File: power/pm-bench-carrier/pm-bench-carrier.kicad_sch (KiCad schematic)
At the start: 41 parts, among them J1 VIN 40-60V, J2 VOUT 19V, Q1 2N7002, X1 PM-19V-200W, X2 Aux socket

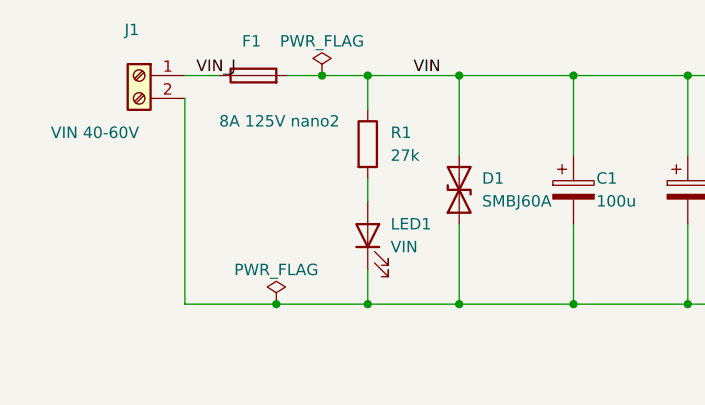
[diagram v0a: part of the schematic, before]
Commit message: pm-bench-carrier: LCSC numbers on the SMD parts, fuse 10 A (0451010.MRL); jlcfab BOM/CPL filled
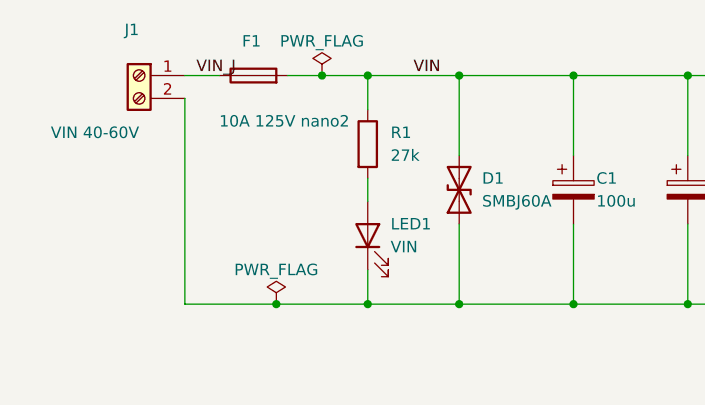
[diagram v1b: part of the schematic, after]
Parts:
- C3: LCSC (none) -> C55151
- C5: LCSC (none) -> C2918502
- C6: LCSC (none) -> C15849
- D1: LCSC (none) -> C353345
- D2: LCSC (none) -> C27131
- F1: value 8A 125V nano2 -> 10A 125V nano2; LCSC (none) -> C44479
- LED1, LED2, LED4: LCSC (none) -> C2297
- LED3: LCSC (none) -> C84256
- Q1: LCSC (none) -> C8545
- R1: LCSC (none) -> C17943
- R2: LCSC (none) -> C17414
- R3: LCSC (none) -> C270956
- R4, R6: LCSC (none) -> C25803
- R5, R7: LCSC (none) -> C22978
- R8, R9: LCSC (none) -> C25804
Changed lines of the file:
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@@
 			)
 		)
-		(property "Value" "8A 125V nano2"
+		(property "Value" "10A 125V nano2"
 			(at 39.37 55.88 270)
 			(show_name no)
@@
 			)
 		)
+		(property "LCSC" "C44479"
+			(at 43.18 50.8 0)
+			(show_name no)
+			(do_not_autoplace no)
+			(hide yes)
+			(effects
+				(font
+					(size 1.27 1.27)
+				)
+			)
+		)
 		(pin "1"
 		)
@@
 			)
 		)
+		(property "LCSC" "C353345"
+			(at 66.04 63.5 0)
+			(show_name no)
+			(do_not_autoplace no)
+			(hide yes)
+			(effects
+				(font
+					(size 1.27 1.27)
+				)
+			)
+		)
 		(pin "1"
 		)
@@
 			)
 		)
+		(property "LCSC" "C55151"
+			(at 101.6 63.5 0)
+			(show_name no)
+			(do_not_autoplace no)
+			(hide yes)
+			(effects
+				(font
+					(size 1.27 1.27)
+				)
+			)
+		)
 		(pin "1"
 		)
@@
 			)
 		)
+		(property "LCSC" "C17943"
+			(at 55.88 58.42 0)
+			(show_name no)
+			(do_not_autoplace no)
+			(hide yes)
+			(effects
+				(font
+					(size 1.27 1.27)
+				)
+			)
+		)
 		(pin "1"
 		)
@@
 			)
 		)
+		(property "LCSC" "C2297"
+			(at 55.88 68.58 0)
+			(show_name no)
+			(do_not_autoplace no)
+			(hide yes)
+			(effects
+				(font
+					(size 1.27 1.27)
+				)
+			)
+		)
 		(pin "1"
 		)
@@
 			)
 		)
+		(property "LCSC" "C2918502"
+			(at 187.96 63.5 0)
+			(show_name no)
+			(do_not_autoplace no)
+			(hide yes)
+			(effects
+				(font
+					(size 1.27 1.27)
+				)
+			)
+		)
 		(pin "1"
 		)
@@
 			)
 		)
+		(property "LCSC" "C17414"
+			(at 198.12 58.42 0)
+			(show_name no)
+			(do_not_autoplace no)
+			(hide yes)
+			(effects
+				(font
+					(size 1.27 1.27)
+				)
+			)
+		)
 		(pin "1"
 		)
@@
 			)
 		)
+		(property "LCSC" "C2297"
+			(at 198.12 68.58 0)
+			(show_name no)
+			(do_not_autoplace no)
+			(hide yes)
+			(effects
+				(font
+					(size 1.27 1.27)
+				)
+			)
+		)
 		(pin "1"
 		)
@@
 			)
 		)
+		(property "LCSC" "C270956"
+			(at 35.56 106.68 0)
+			(show_name no)
+			(do_not_autoplace no)
+			(hide yes)
+			(effects
+				(font
+					(size 1.27 1.27)
+				)
+			)
+		)
 		(pin "1"
 		)
@@
 			)
 		)
+		(property "LCSC" "C27131"
+			(at 35.56 118.11 0)
+			(show_name no)
+			(do_not_autoplace no)
+			(hide yes)
+			(effects
+				(font
+					(size 1.27 1.27)
+				)
+			)
+		)
 		(pin "1"
 		)
@@
 			)
 		)
+		(property "LCSC" "C15849"
+			(at 48.26 118.11 0)
+			(show_name no)
+			(do_not_autoplace no)
+			(hide yes)
+			(effects
+				(font
+					(size 1.27 1.27)
+				)
+			)
+		)
 		(pin "1"
 		)
@@
 			)
 		)
+		(property "LCSC" "C25803"
+			(at 104.14 128.27 0)
+			(show_name no)
+			(do_not_autoplace no)
+			(hide yes)
+			(effects
+				(font
+					(size 1.27 1.27)
+				)
+			)
+		)
 		(pin "1"
 		)
@@
 			)
 		)
+		(property "LCSC" "C22978"
+			(at 114.3 118.11 0)
+			(show_name no)
+			(do_not_autoplace no)
+			(hide yes)
+			(effects
+				(font
+					(size 1.27 1.27)
+				)
+			)
+		)
 		(pin "1"
 		)
@@
 			)
 		)
+		(property "LCSC" "C84256"
+			(at 114.3 127 0)
+			(show_name no)
+			(do_not_autoplace no)
+			(hide yes)
+			(effects
+				(font
+					(size 1.27 1.27)
+				)
+			)
+		)
 		(pin "1"
 		)
@@
 			)
 		)
+		(property "LCSC" "C25803"
+			(at 132.08 128.27 0)
+			(show_name no)
+			(do_not_autoplace no)
+			(hide yes)
+			(effects
+				(font
+					(size 1.27 1.27)
+				)
+			)
+		)
 		(pin "1"
 		)
@@
 			)
 		)
+		(property "LCSC" "C8545"
+			(at 142.24 134.62 0)
+			(show_name no)
+			(do_not_autoplace no)
+			(hide yes)
+			(effects
+				(font
+					(size 1.27 1.27)
+				)
+			)
+		)
 		(pin "1"
 		)
@@
 			)
 		)
+		(property "LCSC" "C2297"
+			(at 144.78 123.19 0)
+			(show_name no)
+			(do_not_autoplace no)
+			(hide yes)
+			(effects
+				(font
+					(size 1.27 1.27)
+				)
+			)
+		)
 		(pin "1"
 		)
@@
 			)
 		)
+		(property "LCSC" "C22978"
+			(at 144.78 113.03 0)
+			(show_name no)
+			(do_not_autoplace no)
+			(hide yes)
+			(effects
+				(font
+					(size 1.27 1.27)
+				)
+			)
+		)
 		(pin "1"
 		)
@@
 			)
 		)
+		(property "LCSC" "C25804"
+			(at 160.02 128.27 0)
+			(show_name no)
+			(do_not_autoplace no)
+			(hide yes)
+			(effects
+				(font
+					(size 1.27 1.27)
+				)
+			)
+		)
 		(pin "1"
 		)
@@
 			(at 177.8 128.27 0)
 			(show_name no)
+			(do_not_autoplace no)
+			(hide yes)
+			(effects
+				(font
+					(size 1.27 1.27)
+				)
+			)
+		)
+		(property "LCSC" "C25804"
+			(at 177.8 128.27 0)
+			(show_name no)

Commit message: pm-bench-carrier schematic: screwed PM mount (SO1-SO4 M2 SMT standoffs S1 VIN / S2 GND / S3 GND / S4 VOUT, PG1-PG6 pogos on A1-A6) replaces the DOSA socket X1 and aux socket X2; sense jumpers JP2/JP3 and TEMP (R9, TP10) removed, RUN on PG4; rev 0.2; ERC 0
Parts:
- removed JP2: SENSE+, Jumper:SolderJumper-2_P1.3mm_Open_RoundedPad1.0x1.5mm, symbol Jumper:SolderJumper_2_Open
- removed JP3: SENSE-, Jumper:SolderJumper-2_P1.3mm_Open_RoundedPad1.0x1.5mm, symbol Jumper:SolderJumper_2_Open
- removed R9: 10k, Resistor_SMD:R_0603_1608Metric, symbol Device:R
- removed TP10: TEMP, TestPoint:TestPoint_Loop_D2.50mm_Drill1.0mm, symbol Connector:TestPoint
- removed X1: PM-19V-200W, carrier:Brick_Eighth_DOSA_Socket, symbol carrier:PM_Brick_Socket
- removed X2: Aux socket, Connector_PinSocket_1.27mm:PinSocket_1x05_P1.27mm_Vertical, symbol Connector_Generic:Conn_01x05
- added PG1: A1 OV_KILL, carrier:PM_Pogo_YZ130115073P, symbol Connector_Generic:Conn_01x01
- added PG2: A2 PGOOD, carrier:PM_Pogo_YZ130115073P, symbol Connector_Generic:Conn_01x01
- added PG3: A3 ID, carrier:PM_Pogo_YZ130115073P, symbol Connector_Generic:Conn_01x01
- added PG4: A4 RUN, carrier:PM_Pogo_YZ130115073P, symbol Connector_Generic:Conn_01x01
- added PG5: A5 GND, carrier:PM_Pogo_YZ130115073P, symbol Connector_Generic:Conn_01x01
- added PG6: A6 GND, carrier:PM_Pogo_YZ130115073P, symbol Connector_Generic:Conn_01x01
- added SO1: S1 VIN, carrier:PM_Standoff_M2x6_SMTSO, symbol Connector_Generic:Conn_01x01
- added SO2: S2 GND, carrier:PM_Standoff_M2x6_SMTSO, symbol Connector_Generic:Conn_01x01
- added SO3: S3 GND, carrier:PM_Standoff_M2x6_SMTSO, symbol Connector_Generic:Conn_01x01
- added SO4: S4 VOUT, carrier:PM_Standoff_M2x6_SMTSO, symbol Connector_Generic:Conn_01x01
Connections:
- net GND: now also PG5.1 (Pin_1), PG6.1 (Pin_1), SO2.1 (Pin_1), SO3.1 (Pin_1)
- net ID: now also PG3.1 (Pin_1)
- net OV_KILL: now also PG1.1 (Pin_1)
- net PGOOD: now also PG2.1 (Pin_1)
- net RUN: now also PG4.1 (Pin_1)
- net VIN: now also SO1.1 (Pin_1)
- net VOUT: now also SO4.1 (Pin_1)
- no-connect marks 1 -> 0
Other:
- note added: "Bench carrier for the screwed PM modules (PM-19V-250W; mount and contacts per docs/pm-interface.md)."
- note added: "J1: lab supply 40-60 V, current limit ~6 A. J2: electronic load, set its OVP to ~22 V. 13.2 A continuous (250 W)."
- note added: "OV LED lit = OV_KILL low (module output overvoltage). PGOOD LED lit = PGOOD high. ID reads against 10k to +5V (22k = PM-19V-250W)."
- note added: "PG1-PG6: pogo pins (C5157258) on the module aux pads A1-A6 (OV_KILL, PGOOD, ID, RUN, GND, GND)."
- note added: "SO1-SO4: M2 x 6 SMT standoffs (C2915628), screws S1 VIN, S2 GND in, S3 GND out, S4 VOUT; they carry the power."
- note added: "TP1-TP4: Kelvin points at the standoffs for efficiency measurement. VIN/VOUT LEDs show the rails."
- note removed: "9372 (1.14-1.65 mm pins, 2.64 mm hole, 18 A) on 4 and 8. X2: 1.27 mm socket for the module aux row (J2)."
- note removed: "Bench carrier for the PM-19V-200W port module (and, with JP2/JP3 closed, an off-the-shelf DOSA eighth brick)."
- note removed: "J1: lab supply 40-60 V, current limit ~6 A. J2: electronic load, set its OVP to ~22 V. 10.5 A continuous."
- note removed: "OV LED lit = OV_KILL low (module output overvoltage). PGOOD LED lit = PGOOD high. ID/TEMP read against 10k to +5V."
- note removed: "TP1-TP4: Kelvin points at the socket pins for efficiency measurement. VIN/VOUT LEDs show the rails."
- note removed: "X1: 8 Mill-Max solder-mount receptacles in the DOSA pattern: 0331 (0.94-1.09 mm pins, 1.85 mm hole) on 1-3, 5-7;"
- title: PM-19V-200W bench carrier -> PM module bench carrier

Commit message: PM aux contacts: 2x3 1.27 mm SMT header (module J2, C41376035) into SMT socket (carrier J3, C41397112) replaces flat pads + pogos; standoffs M2 x 7 (C2916355), gap 7.0 mm. pmmount.py generates the new footprints; module J2 swapped in place, tools/route_aux.py moves PGOOD's via and adds a GND via between the columns (DRC as before, 0 unconnected, parity clean); carrier PG1-PG6 -> J3 and rebuilt by its flow (DRC 0 errors, 0 unconnected, parity clean); spec, ADR 0003 (6, 7), power-board.md and handoff updated; ID open = slot fault rule
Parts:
- removed PG1: A1 OV_KILL, carrier:PM_Pogo_YZ130115073P, symbol Connector_Generic:Conn_01x01
- removed PG2: A2 PGOOD, carrier:PM_Pogo_YZ130115073P, symbol Connector_Generic:Conn_01x01
- removed PG3: A3 ID, carrier:PM_Pogo_YZ130115073P, symbol Connector_Generic:Conn_01x01
- removed PG4: A4 RUN, carrier:PM_Pogo_YZ130115073P, symbol Connector_Generic:Conn_01x01
- removed PG5: A5 GND, carrier:PM_Pogo_YZ130115073P, symbol Connector_Generic:Conn_01x01
- removed PG6: A6 GND, carrier:PM_Pogo_YZ130115073P, symbol Connector_Generic:Conn_01x01
- added J3: Aux socket 2x3 1.27, carrier:PM_Aux_Socket_2x03_P1.27, symbol Connector_Generic:Conn_01x06
- SO1, SO2, SO3, SO4: footprint carrier:PM_Standoff_M2x6_SMTSO -> carrier:PM_Standoff_M2x7_SMTSO; LCSC C2915628 -> C2916355
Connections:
- net GND: now also J3.5 (Pin_5), J3.6 (Pin_6)
- net ID: now also J3.3 (Pin_3)
- net OV_KILL: now also J3.1 (Pin_1)
- net PGOOD: now also J3.2 (Pin_2)
- net RUN: now also J3.4 (Pin_4)
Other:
- note added: "J3: 2x3 1.27 mm SMT socket (C41397112), the module aux header plugs in; pin n = An (OV_KILL, PGOOD, ID, RUN, GND, GND)."
- note added: "SO1-SO4: M2 x 7 SMT standoffs (C2916355, 7.0 mm module gap), screws S1 VIN, S2 GND in, S3 GND out, S4 VOUT; they carry the power."
- note removed: "PG1-PG6: pogo pins (C5157258) on the module aux pads A1-A6 (OV_KILL, PGOOD, ID, RUN, GND, GND)."
- note removed: "SO1-SO4: M2 x 6 SMT standoffs (C2915628), screws S1 VIN, S2 GND in, S3 GND out, S4 VOUT; they carry the power."

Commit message: 3D models: module aux header J2 on pm-19v-250w (hanxia HX PZ1.27-2x3P TP, C41376035; on B, offset sign follows the flip); unit U5 (stock VQFN-32 footprint points at a STEP KiCad does not ship: pp48 copy with the stock QFN-32 5x5 EP3.3 body), J201 XT60 (C98732), photoMOS U6 / U7 / U56 / U57 TLP176AM (C5370540) and opto U8 / U58 TLP291 (C55144, turned to its pin-1 dot) as pp48 footprint copies (stock models missing), FPIDs moved in uinput.py / unit.py and the board; carrier F1 nano2 fuse (C44479) as a carrier footprint copy; placement = pad fit of the LCSC footprint + the STEP-to-WRL origin shift (EasyEDA STEPs are not on the footprint origin, checked against the XT30 of 020591f), which also corrects today's aux socket (+0.3 mm z) and Degson terminal (-0.1 y, +0.2 z); renders checked; ERC 0 and DRC counts unchanged on unit, carrier, module
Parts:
- F1: footprint Fuse:Fuse_Littelfuse-NANO2-451_453 -> carrier:Fuse_Littelfuse-NANO2-451_453
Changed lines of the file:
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@@
 			)
 		)
-		(property "Footprint" "Fuse:Fuse_Littelfuse-NANO2-451_453"
+		(property "Footprint" "carrier:Fuse_Littelfuse-NANO2-451_453"
 			(at 43.18 50.8 0)
 			(show_name no)
